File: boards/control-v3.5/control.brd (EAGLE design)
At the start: 136.5 x 115.2 mm, 225 parts, among them IC1 MCP23017-E/SS, J1 HFW8R-1ST, J2 HFW8R-1ST, J3 6-PIN_2MM-H, J4 HFW8R-1ST, J5 2-PIN-KICKERS, J6 DF22-2, M1:C1 1uF, M1:C10 0.1uF 50V, M1:C12 ECA-1HHG221, M1:C13 ECA-1HHG221, M1:C2 1uF, M1:C3 0.022uF 50V, M1:C6 0.1uF 50V, M1:C7 0.1uF 50V, M1:C8 0.1uF 50V, M1:C9 2.2uF 50V, M1:J1 MKS-1658, M1:J2 4-PIN_2MM-H, M1:Q1 IRFH7545, M1:Q2 IRFH7545, M1:Q3 IRFH7545, M1:Q4 IRFH7545, M1:Q5 IRFH7545, M1:Q6 IRFH7545, M1:R1 10k, M1:U1 DRV8303DCA, M2:C1 1uF, M2:C10 0.1uF 50V, M2:C12 ECA-1HHG221, M2:C13 ECA-1HHG221, M2:C2 1uF, M2:C3 0.022uF 50V, M2:C6 0.1uF 50V, M2:C7 0.1uF 50V, M2:C8 0.1uF 50V, M2:C9 2.2uF 50V, M2:J1 MKS-1658, M2:J2 4-PIN_2MM-H, M2:Q1 IRFH7545, M2:Q2 IRFH7545, M2:Q3 IRFH7545, M2:Q4 IRFH7545, M2:Q5 IRFH7545, M2:Q6 IRFH7545, M2:R1 10k, M2:U1 DRV8303DCA, M3:C1 1uF, M3:C10 0.1uF 50V, M3:C12 ECA-1HHG221, M3:C13 ECA-1HHG221, M3:C2 1uF, M3:C3 0.022uF 50V, M3:C6 0.1uF 50V, M3:C7 0.1uF 50V, M3:C8 0.1uF 50V, M3:C9 2.2uF 50V, M3:J1 MKS-1658, M3:J2 4-PIN_2MM-H, M3:Q1 IRFH7545, M3:Q2 IRFH7545, M3:Q3 IRFH7545, M3:Q4 IRFH7545, M3:Q5 IRFH7545, M3:Q6 IRFH7545, M3:R1 10k, M3:U1 DRV8303DCA, M4:C1 1uF, M4:C10 0.1uF 50V, M4:C12 ECA-1HHG221, M4:C13 ECA-1HHG221, M4:C2 1uF, M4:C3 0.022uF 50V, M4:C6 0.1uF 50V, M4:C7 0.1uF 50V, M4:C8 0.1uF 50V, M4:C9 2.2uF 50V, M4:J1 MKS-1658, M4:J2 4-PIN_2MM-H, M4:Q1 IRFH7545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

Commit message: schematic progress
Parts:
- added C31: 330uF, rcl:D/7343-31R
- added C32, C33, C34, C35, C36, C37, C52, C53, C60, C73, C74, C75, C78, C79, C82, C83: 4.7uF, rcl:C0603
- added C38, C39, C40, C41, C42, C43, C44, C45, C47, C48, C49, C50, C51, C61, C62, C63, C64, C65, C66, C67, C68, C69, C70, C71, C72, C76, C77, C80, C81: 0.47uF, rcl:C0603
- added C46: 100uF, rcl:C1210
- added C54, C55, C56, C57, C58, C59: 47uF, rcl:C0805
- U2: device RoboJackets-ICs:SOT23-5 -> RoboJackets-ICs:SOT-23-5
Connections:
- removed net VCCAUX: U8.G10, U8.J10, U8.K11, U8.L10
- removed net VCCBRAM: U8.E10, U8.F11
- removed net VCCINT: U8.F7, U8.F9, U8.G6, U8.H9, U8.J6, U8.K9, U8.L8
- removed net VCCO_0: U8.L6
- removed net VCCO_14: U8.L16, U8.M13, U8.N10, U8.P7, U8.R14, U8.T11
- removed net VCCO_15: U8.A16, U8.B13, U8.C10, U8.E14, U8.H15, U8.J12
- removed net VCCO_34: U8.M3, U8.R4, U8.T1
- removed net VCCO_35: U8.A6, U8.B3, U8.D7, U8.E4, U8.F1, U8.J2
- new net +1.0V: C31.+, C32.1, C33.1, C34.1, C35.1, C36.1, C37.1, C38.1, C39.1, C40.1, C41.1, C42.1, C43.1, C44.1, C45.1, C46.1, C47.1, C48.1, U8.E10, U8.F11, U8.F7, U8.F9, U8.G6, U8.H9, U8.J6, U8.K9, U8.L8
- new net +1.8V: C49.1, C50.1, C51.1, C52.1, C53.1, C54.1, U8.G10, U8.J10, U8.K11, U8.L10
- new net N$10: C56.2, C61.2, C65.2, C80.2, C81.2, C82.2, C83.2
- new net N$6: C56.1, C61.1, C65.1, C80.1, C81.1, C82.1, C83.1, U8.L16, U8.M13, U8.N10, U8.P7, U8.R14, U8.T11
- net +3.3V: now also C55.1, C57.1, C58.1, C59.1, C60.1, C62.1, C63.1, C64.1, C66.1, C67.1, C68.1, C69.1, C70.1, C71.1, C72.1, C73.1, C74.1, C75.1, C76.1, C77.1, C78.1, C79.1, U8.A16, U8.A6, U8.B13, U8.B3, U8.C10, U8.D7, U8.E14, U8.E4, U8.F1, U8.H15, U8.J12, U8.J2, U8.L6, U8.M3, U8.R4, U8.T1
- net GND: now also C31.-, C32.2, C33.2, C34.2, C35.2, C36.2, C37.2, C38.2, C39.2, C40.2, C41.2, C42.2, C43.2, C44.2, C45.2, C46.2, C47.2, C48.2, C49.2, C50.2, C51.2, C52.2, C53.2, C54.2, C55.2, C57.2, C58.2, C59.2, C60.2, C62.2, C63.2, C64.2, C66.2, C67.2, C68.2, C69.2, C70.2, C71.2, C72.2, C73.2, C74.2, C75.2, C76.2, C77.2, C78.2, C79.2

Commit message: Power FPGA done, need to add missing power sources, prog fpga in progress
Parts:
- removed C10, C11, C12, C13, C14, C15, C16, C17, C19, C20, C21, C7, C9: 0.1uF, resistor:C0603
- removed R10: 330, resistor:R0603
- removed R11, R9: 4.7k, resistor:R0603
- added L1, L2: 60Ohm@100MHz, RoboJackets-Inductors:L0603
- C4: device resistor:C0603 -> rcl:C0603
- C6: value 0.1uF -> 0.47uF; device resistor:C0603 -> rcl:C0603
- moved C6 459.4 mm to (-106.0, -432.0), flipped to the top, turned to 0 degrees
- moved C4 446.8 mm to (-106.0, -417.0), flipped to the top, turned to 0 degrees
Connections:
- removed net +1.8V: C49.1, C50.1, C51.1, C52.1, C53.1, C54.1, U8.G10, U8.J10, U8.K11, U8.L10
- removed net GNDADC_0: U8.G7
- removed net VCCADC_0: U8.G8
- removed net VCCBATT_0: U8.F8
- new net GNDADC: C4.2, C6.2, L1.1, U8.G7, U8.H7, U8.J8
- new net VCCAUX: C4.1, C49.1, C50.1, C51.1, C52.1, C53.1, C54.1, C6.1, L2.1, L2.2, U8.G10, U8.G8, U8.J10, U8.K11, U8.L10
- net +1.2V: no longer C10.1, C14.1, C19.1, C6.1, U1.115, U1.45, U1.80, U1.9
- net +2.5V: no longer C15.1, C20.1, C4.1, C9.1, R10.2, R9.2, U1.102, U1.137, U1.30, U1.65
- net +3.3V: no longer C11.1, C12.1, C13.1, C16.1, C17.1, C21.1, C7.1, R11.1, U1.100, U1.121, U1.13, U1.138, U1.28, U1.42, U1.49, U1.79
- net FPGA-DONE: now also U8.H10; no longer R10.1, U1.72
- net FPGA-INIT: now also U8.K10; no longer R11.2, U1.40
- net FPGA-PROG: now also U8.L9; no longer R9.1, U1.1
- net GND: now also L1.2, U8.F8, U8.H8, U8.J7, U8.K7, U8.K8; no longer C10.2, C11.2, C12.2, C13.2, C14.2, C15.2, C16.2, C17.2, C19.2, C20.2, C21.2, C4.2, C6.2, C7.2, C9.2, U1.11, U1.118, U1.127, U1.133, U1.19, U1.27, U1.37, U1.46, U1.55, U1.61, U1.73, U1.90, U1.99
- net MOSI-FPGA: now also U8.J13; no longer U1.63
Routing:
- net GND: track 387.8 -> 336.8 mm, vias 198 -> 176
- net +3.3V: track 133.4 -> 99.9 mm, vias 34 -> 26
- net +1.2V: track 119.4 -> 100.8 mm, vias 8 -> 5
- net +2.5V: track 175.1 -> 164.9 mm
- net FPGA-INIT: track 46.3 -> 41.1 mm, vias 2 -> 1
- net MOSI-FPGA: track 46.9 -> 45.2 mm
- net FPGA-PROG: track 66.1 -> 65.1 mm

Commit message: Schematic progress, prog almost wired, started on io banks
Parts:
- removed C18: 0.1uF, resistor:C0603
- added R10, R9: 4.7k, rcl:R0603
- added R11: 330, rcl:R0603
- moved U8 140.0 mm to (0.00, 23.0)
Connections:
- removed net R-P41: RN2.1, U1.5
- removed net R-P42: RN2.2, U1.4
- removed net R-P43: RN2.3, U1.3
- removed net R-P44: RN2.4, U1.2
- removed net R-P45: RN2.5, U1.142
- removed net R-P46: RN2.6, U1.141
- removed net R-P47: RN2.7, U1.140
- removed net R-P48: RN2.8, U1.139
- removed net R-P57: RN7.1, U1.35
- removed net R-P58: RN7.2, U1.34
- removed net R-P59: RN7.3, U1.32
- removed net R-P60: RN7.4, U1.31
- removed net R-P61: RN7.5, U1.26
- removed net R-P62: RN7.6, U1.25
- removed net R-P63: RN7.7, U1.24
- removed net R-P64: RN7.8, U1.23
- new net +1.8V: L2.2
- new net T1: RN2.1, U8.M16
- new net T10: RN7.2, U8.A13
- new net T11: RN7.3, U8.A14
- new net T12: RN7.8, U8.C14
- new net T13: RN7.7, U8.B14
- new net T14: RN7.6, U8.B15
- new net T15: RN7.4, U8.A15
- new net T16: RN7.5, U8.B16
- new net T2: RN2.2, U8.N16
- new net T3: RN2.4, U8.P15
- new net T4: RN2.3, U8.P16
- new net T5: RN2.6, U8.R15
- new net T6: RN2.5, U8.R16
- new net T7: RN2.8, U8.T14
- new net T8: RN2.7, U8.T15
- new net T9: RN7.1, U8.A12
- new net VCCO_0: C22.1, C23.1, C5.1, C55.1, C57.1, C58.1, C59.1, C60.1, C62.1, C63.1, C64.1, C66.1, C67.1, C68.1, C69.1, C70.1, C71.1, C72.1, C73.1, C74.1, C75.1, C76.1, C77.1, C78.1, C79.1, C8.1, D1.A, D10.A, D5.A, D6.A, D7.A, D8.A, D9.A, DD:C1.1, DD:C10.1, DD:R1.1, DD:U1.19, DD:U1.45, IC1.15, IC1.18, IC1.9, J1.6, J4.7, KIT2.8, R12.2, R30.2, R33.1, R5.2, R6.2, U1.143, U2.5, U6.1, U6.3, U7.1, U7.3, U8.A16, U8.A6, U8.B13, U8.B3, U8.C10, U8.D7, U8.E14, U8.E4, U8.F1, U8.H15, U8.J12, U8.J2, U8.L6, U8.M3, U8.R4, U8.T1, X1.1, X1.4
- net !CS!-FPGA: now also U8.K12; no longer U1.69
- net +3.3V: now also R10.2, R11.2, R9.2, U8.E7, U8.M10, U8.M11, U8.M9; no longer C18.1, C22.1, C23.1, C5.1, C55.1, C57.1, C58.1, C59.1, C60.1, C62.1, C63.1, C64.1, C66.1, C67.1, C68.1, C69.1, C70.1, C71.1, C72.1, C73.1, C74.1, C75.1, C76.1, C77.1, C78.1, C79.1, C8.1, D1.A, D10.A, D5.A, D6.A, D7.A, D8.A, D9.A, DD:C1.1, DD:C10.1, DD:R1.1, DD:U1.19, DD:U1.45, IC1.15, IC1.18, IC1.9, J1.6, J4.7, KIT2.8, R12.2, R30.2, R33.1, R5.2, R6.2, U1.143, U1.57, U1.60, U1.62, U1.64, U2.5, U6.1, U6.3, U7.1, U7.3, U8.A16, U8.A6, U8.B13, U8.B3, U8.C10, U8.D7, U8.E14, U8.E4, U8.F1, U8.H15, U8.J12, U8.J2, U8.L6, U8.M3, U8.R4, U8.T1, X1.1, X1.4
- net FPGA-DONE: now also R11.1
- net FPGA-INIT: now also R9.1
- net FPGA-PROG: now also R10.1
- net GND: now also U8.L15; no longer C18.2
- net MISO-FPGA: now also U8.J13; no longer U1.44
- net MOSI-FPGA: now also U8.J14; no longer U8.J13
- net SCK-FPGA: now also U8.E8; no longer U1.71
- net VCCAUX: no longer L2.2
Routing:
- net +3.3V: track 99.9 -> 0.00 mm, vias 26 -> 0
- net VCCO_0: track 0.00 -> 86.6 mm, vias 0 -> 25
- net R-P48: track 6.79 -> 0.00 mm
- net R-P47: track 6.54 -> 0.00 mm
- net R-P41: track 6.45 -> 0.00 mm
- net R-P46: track 6.29 -> 0.00 mm
- net R-P42: track 6.20 -> 0.00 mm
- net R-P45: track 6.04 -> 0.00 mm
- net R-P43: track 5.95 -> 0.00 mm
- net R-P44: track 5.70 -> 0.00 mm
- net R-P61: track 3.45 -> 0.00 mm
- net R-P60: track 3.45 -> 0.00 mm
- net R-P58: track 3.41 -> 0.00 mm
- net R-P62: track 3.33 -> 0.00 mm
- net R-P59: track 3.33 -> 0.00 mm
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- added copper zone on layer 16, net VCCO_0
- added copper zone on layer 3, net VCCO_0
- removed copper zone on layer 16, net +3.3V
- removed copper zone on layer 3, net +3.3V

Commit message: IOs for motors all linked, still need external clock, power line and battery status wiring
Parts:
- removed C5, C8: 0.1uF, resistor:C0603
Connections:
- removed net R-P1: RN8.1, U1.82
- removed net R-P10: RN6.2, U1.89
- removed net R-P11: RN6.3, U1.88
- removed net R-P12: RN6.4, U1.87
- removed net R-P13: RN6.5, U1.86
- removed net R-P14: RN6.6, U1.85
- removed net R-P15: RN6.7, U1.84
- removed net R-P16: RN6.8, U1.83
- removed net R-P17: RN5.1, U1.101
- removed net R-P18: RN5.2, U1.98
- removed net R-P19: RN5.3, U1.97
- removed net R-P2: RN8.2, U1.81
- removed net R-P20: RN5.4, U1.96
- removed net R-P21: RN5.5, U1.95
- removed net R-P22: RN5.6, U1.94
- removed net R-P23: RN5.7, U1.93
- removed net R-P24: RN5.8, U1.92
- removed net R-P25: RN3.1, U1.117
- removed net R-P26: RN3.2, U1.116
- removed net R-P27: RN3.3, U1.113
- removed net R-P28: RN3.4, U1.112
- removed net R-P29: RN3.5, U1.106
- removed net R-P3: RN8.3, U1.77
- removed net R-P30: RN3.6, U1.105
- removed net R-P31: RN3.7, U1.104
- removed net R-P32: RN3.8, U1.103
- removed net R-P36: RN1.4, U1.125
- removed net R-P37: RN1.5, U1.124
- removed net R-P38: RN1.6, U1.123
- removed net R-P39: RN1.7, U1.122
- removed net R-P4: RN8.4, U1.76
- removed net R-P40: RN1.8, U1.119
- removed net R-P49: RN4.1, U1.21
- removed net R-P5: RN8.5, U1.75
- removed net R-P50: RN4.2, U1.20
- removed net R-P51: RN4.3, U1.17
- removed net R-P52: RN4.4, U1.16
- removed net R-P53: RN4.5, U1.15
- removed net R-P54: RN4.6, U1.14
- removed net R-P55: RN4.7, U1.8
- removed net R-P56: RN4.8, U1.7
- removed net R-P6: RN8.6, U1.74
- removed net R-P7: RN8.7, U1.70
- removed net R-P8: RN8.8, U1.68
- removed net R-P9: RN6.1, U1.91
- new net T17: RN4.8, U8.J16
- new net T18: RN4.7, U8.J15
- new net T19: RN4.5, U8.G16
- new net T20: RN4.6, U8.H16
- new net T21: RN4.2, U8.E15
- new net T22: RN4.4, U8.F15
- new net T23: RN4.1, U8.D16
- new net T24: RN4.3, U8.E16
- new net T25: RN8.8, U8.A5
- new net T26: RN8.7, U8.A4
- new net T27: RN8.6, U8.A3
- new net T28: RN8.2, U8.C2
- new net T29: RN8.4, U8.B2
- new net T30: RN8.5, U8.A2
- new net T31: RN8.1, U8.C1
- new net T32: RN8.3, U8.B1
- new net T33: RN6.8, U8.C3
- new net T34: RN6.6, U8.E2
- new net T35: RN6.7, U8.D1
- new net T36: RN6.1, U8.H1
- new net T37: RN6.2, U8.G1
- new net T38: RN6.3, U8.G2
- new net T39: RN6.5, U8.E1
- new net T40: RN6.4, U8.F2
- new net T41: RN5.6, U8.K2
- new net T42: RN5.4, U8.L2
- new net T43: RN5.7, U8.J1
- new net T44: RN5.5, U8.K1
- new net T45: RN5.8, U8.H2
- new net T46: RN5.3, U8.M2
- new net T47: RN5.2, U8.M1
- new net T48: RN5.1, U8.N1
- new net T49: RN3.2, U8.T3
- new net T50: RN3.1, U8.T4
- new net T51: RN3.3, U8.T2
- new net T52: RN3.4, U8.R3
- new net T53: RN3.5, U8.R1
- new net T54: RN3.6, U8.R2
- new net T55: RN3.7, U8.P1
- new net T56: RN3.8, U8.N2
- new net T57: RN1.8, U8.T5
- new net T58: RN1.4, U8.T10
- new net T59: RN1.5, U8.T9
- new net T60: RN1.6, U8.T8
- new net T61: RN1.7, U8.T7
- net BATT-FPGA: no longer U1.136
- net GND: no longer C5.2, C8.2
- net VCCO_0: no longer C5.1, C8.1, U1.143
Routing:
- net MOSI-FPGA: track 45.2 -> 0.00 mm
- net MISO-FPGA: track 43.7 -> 0.00 mm
- net BATT-FPGA: track 15.6 -> 4.50 mm
- net R-P8: track 9.48 -> 0.00 mm
- net SCK-FPGA: track 50.2 -> 41.4 mm, vias 1 -> 0
- net R-P7: track 8.15 -> 0.00 mm
- net R-P25: track 8.10 -> 0.00 mm
- net R-P26: track 7.86 -> 0.00 mm
- net R-P32: track 7.25 -> 0.00 mm
- net R-P31: track 6.95 -> 0.00 mm
- net R-P27: track 6.77 -> 0.00 mm
- net R-P30: track 6.70 -> 0.00 mm
- net R-P29: track 6.45 -> 0.00 mm
- net R-P28: track 6.44 -> 0.00 mm
- net R-P2: track 6.05 -> 0.00 mm
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
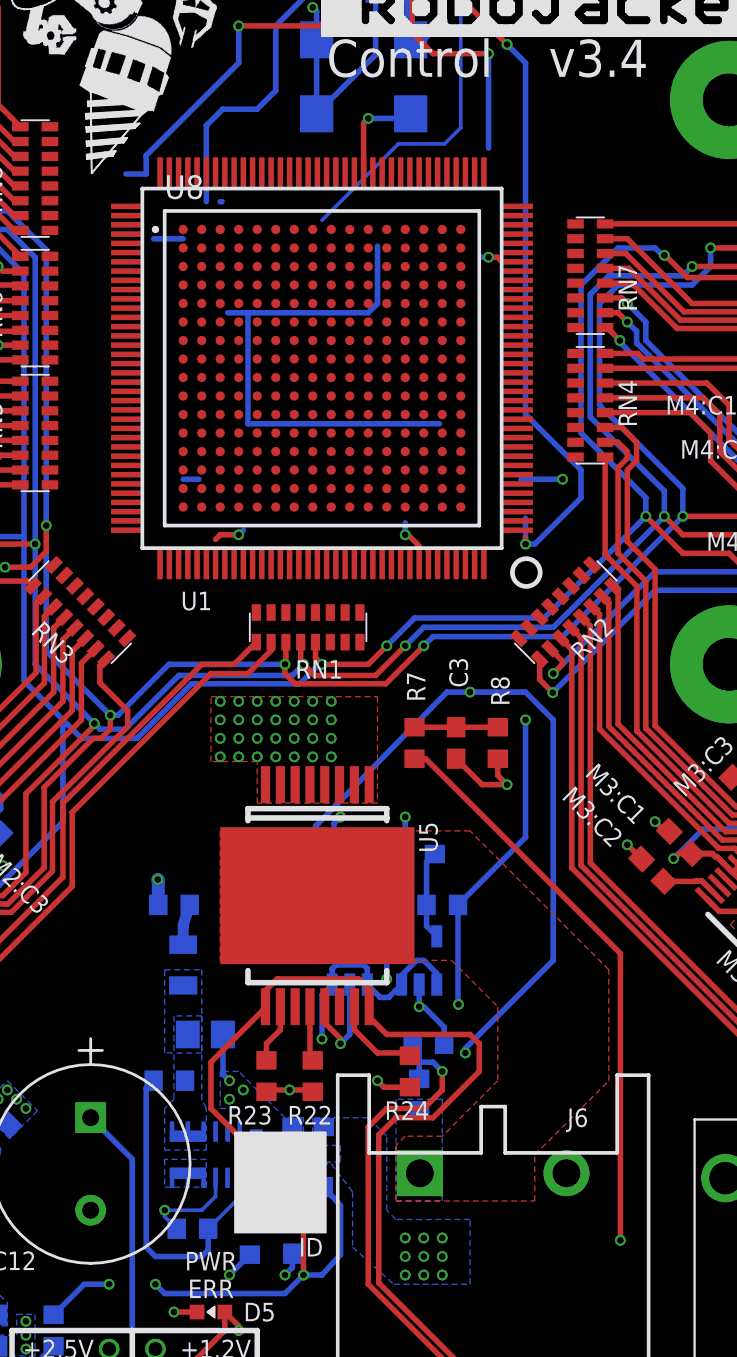
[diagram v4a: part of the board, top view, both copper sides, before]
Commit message: Organized IOs, new clock missing, adding power lines
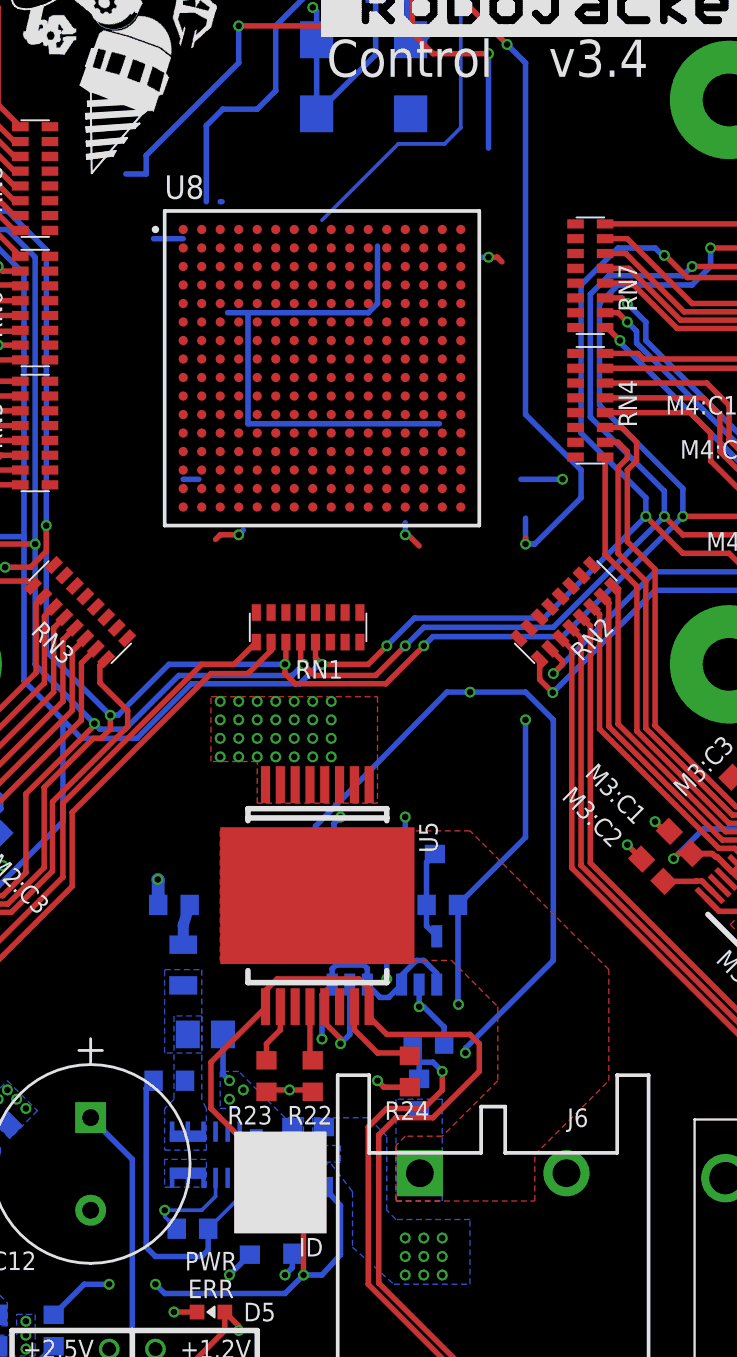
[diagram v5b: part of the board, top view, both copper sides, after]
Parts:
- removed C3: 0.1uF, resistor:C0603
- removed R7: 68k, resistor:R0603
- removed R8: 10k, resistor:R0603
- removed U1: XC3S250E-4TQG144C, RoboJackets-ICs:TQFP144
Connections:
- removed net BATT-FPGA: C3.1, R7.2, R8.1
- removed net FPGA-CLK: U1.50, X1.3
- net +18.5V: no longer R7.1
- net GND: no longer C3.2, R8.2
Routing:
- net +18.5V: track 123.1 -> 92.1 mm, vias 67 -> 66
- net FPGA-CLK: track 5.40 -> 0.00 mm, vias 1 -> 0
- net GND: track 333.1 -> 328.2 mm, vias 174 -> 173
- net BATT-FPGA: track 4.50 -> 0.00 mm

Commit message: FPGA board schematic ready for review!
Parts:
- removed C29: 2.2uF 50V, resistor:C0603
- removed D5: RED, RoboJackets-LEDs:CHIP-LED0603
- removed R34: 0, resistor:R0603
- removed U6: MCP1824T-1202E/OT, RoboJackets-PowerICs:SOT-23-5
- removed U7: MCP1824T-2502E/OT, RoboJackets-PowerICs:SOT-23-5
- added C3, C8: 1uF, resistor:C0603
- added C5, C7: 1uF X7R, resistor:C0603
- added R7: 0, resistor:R0603
- added U$17: MIC47100-1.0YML-TR, RoboJackets-PowerICs:DFN8_2X2MM
- added U1: MCP1824T-1802E/OT, RoboJackets-PowerICs:SOT-23-5
- X1: value ASV-18.432MHZ-EJ-T -> ASV-50.000MHZ-E-T
- moved X1 496.1 mm to (-112.0, -444.0), flipped to the top, turned to 0 degrees
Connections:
- removed net +1.2V: R34.2
- removed net +1.2V-PRE: C29.1, R34.1, U6.5
- removed net +2.5V: R35.2
- removed net +2.5V-PRE: C30.1, R35.1, U7.5
- new net EXT_SCK: U8.A9, X1.3
- new net N$3: C5.1, R7.1, U$17.P$7, U$17.P$8, U$17.P$9
- new net V_OUT: C30.1, R35.1, U1.5
- net +1.0V: now also R7.2
- net +1.8V: now also R35.2
- net +3.3V: now also C3.1, C7.1, C8.1, U$17.P$2, U$17.P$5, U$17.P$6
- net GND: now also C3.2, C5.2, C7.2, C8.2, U$17.P$4, U1.2; no longer C29.2, U6.2, U7.2
- net PWR-ERR: now also U1.4; no longer D5.C, U6.4, U7.4
- net VCCO_0: now also U1.1, U1.3; no longer D5.A, U6.1, U6.3, U7.1, U7.3
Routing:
- net +2.5V: track 162.3 -> 2.55 mm, vias 6 -> 0
- net +1.2V: track 100.8 -> 27.8 mm, vias 4 -> 0
- net PWR-ERR: track 30.0 -> 0.00 mm, vias 2 -> 0
- net VCCO_0: track 81.6 -> 60.6 mm, vias 23 -> 20
- net GND: track 328.2 -> 319.8 mm, vias 173 -> 171
- net +1.2V-PRE: track 4.86 -> 0.00 mm
- net +2.5V-PRE: track 4.49 -> 0.00 mm
- net V_OUT: track 0.00 -> 2.89 mm

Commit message: some modif
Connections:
- net !CS!-IR renamed !CS!-WHISKERS
- net !CS!-RAD0 renamed !CS!-RADIO
- net !RST!-IR renamed !RST!-WHISKERS
- net INT-RAD0 renamed INT-RADIO
- removed net N$10: C56.2, C61.2, C65.2, C80.2, C81.2, C82.2, C83.2
- removed net N$6: C56.1, C61.1, C65.1, C80.1, C81.1, C82.1, C83.1, U8.L16, U8.M13, U8.N10, U8.P7, U8.R14, U8.T11
- net +3.3V: now also C56.1, C61.1, C65.1, C80.1, C81.1, C82.1, C83.1, U8.L16, U8.M13, U8.N10, U8.P7, U8.R14, U8.T11
- net GND: now also C56.2, C61.2, C65.2, C80.2, C81.2, C82.2, C83.2

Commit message: moved clock to sheet 3, removed busses in favor to individual signals
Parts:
- KIT2: value IMUIMU-KIT -> IMU; device RoboJackets-Boards:IMU-KIT -> RoboJackets-Boards:IMU
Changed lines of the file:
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@@
 <attribute name="VALUE" x="-19.29605" y="-17.601975" size="1.27" layer="28" rot="MR135"/>
 </element>
-<element name="KIT2" library="RoboJackets-Boards" package="IMU-KIT" value="IMUIMU-KIT" x="2.223" y="57.5" smashed="yes" rot="R90">
+<element name="KIT2" library="RoboJackets-Boards" package="IMU" value="IMU" x="2.223" y="57.5" smashed="yes" rot="R90">
 <attribute name="VALUE" x="8.843" y="49.88" size="1" layer="27" rot="R90" align="top-left"/>
 </element>
